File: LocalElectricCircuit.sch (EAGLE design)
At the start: 43 parts, among them IC1 PIC32MX360F512L, J1 Prog. Port, J3 Prog. Port, T1 PN100, U1 ADS1118, U2 ADS1118

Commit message: 🗡️🗡️🗡️
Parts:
- added PIC16_POWER_EN, PIC32_POWER_EN: (no value), pinhead:PINHD-1X2
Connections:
- removed net +3V3_PROG: J1.2, R3.1
- new net PIC32_3V3: C1.1, C12.1, C13.1, C14.1, C15.1, C16.1, C2.1, C4.1, C5.1, C6.1, IC1.VDD@1, IC1.VDD@2, IC1.VDD@3, IC1.VDD@4, IC1.VDD@5, J1.2, PIC32_POWER_EN.1, R2.1, R3.1
- net +3V3: now also PIC16_POWER_EN.2, PIC32_POWER_EN.2; no longer C1.1, C12.1, C13.1, C14.1, C15.1, C16.1, C2.1, C4.1, C5.1, C6.1, IC1.VDD@1, IC1.VDD@2, IC1.VDD@3, IC1.VDD@4, IC1.VDD@5, R2.1
- net PIC16_3V3: now also PIC16_POWER_EN.1

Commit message: GND planes and some layout bizz
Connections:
- removed net GND_I_1: J2.A5
- removed net GND_I_2: J2.A6
- removed net GND_I_3: J2.A7
- removed net GND_PROBE: J2.B11, J2.B12, J2.B13, U1.AIN3, U2.AIN3
- new net GND: J2.A5, J2.A6, J2.A7, J2.B11, J2.B12, J2.B13, U1.AIN3, U2.AIN3
- new net PIC_3V3: IC1.VREG
- net +3V3: no longer IC1.VREG
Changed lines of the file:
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@@
 <setting verticaltext="up"/>
 </settings>
-<grid distance="0.1" unitdist="inch" unit="inch" style="lines" multiple="1" display="no" altdistance="0.025" altunitdist="inch" altunit="inch"/>
+<grid distance="0.1" unitdist="inch" unit="inch" style="lines" multiple="1" display="no" altdistance="0.01" altunitdist="inch" altunit="inch"/>
 <layers>
 <layer number="1" name="Top" color="4" fill="1" visible="no" active="no"/>
@@
 </segment>
 <segment>
-<pinref part="IC1" gate="G$1" pin="VREG"/>
-<wire x1="76.2" y1="114.3" x2="76.2" y2="124.46" width="0.1524" layer="91"/>
-<label x="76.835" y="124.46" size="1.778" layer="95" rot="R90"/>
-</segment>
-<segment>
 <pinref part="J2" gate="G$1" pin="B1"/>
 <wire x1="-45.72" y1="172.72" x2="-55.88" y2="172.72" width="0.1524" layer="91"/>
@@
 </segment>
 </net>
-<net name="GND_I_1" class="0">
+<net name="I_1_L" class="0">
+<segment>
+<pinref part="J2" gate="G$1" pin="B5"/>
+<wire x1="-45.72" y1="142.24" x2="-76.2" y2="142.24" width="0.1524" layer="91"/>
+<label x="-76.2" y="142.875" size="1.778" layer="95" rot="R180"/>
+</segment>
+<segment>
+<pinref part="IC1" gate="G$1" pin="RB4"/>
+<wire x1="17.78" y1="40.64" x2="7.62" y2="40.64" width="0.1524" layer="91"/>
+<label x="0" y="40.64" size="1.778" layer="95"/>
+</segment>
+</net>
+<net name="I_1_H" class="0">
+<segment>
+<pinref part="J2" gate="G$1" pin="C5"/>
+<wire x1="-45.72" y1="139.7" x2="-76.2" y2="139.7" width="0.1524" layer="91"/>
+<label x="-76.2" y="140.335" size="1.778" layer="95" rot="R180"/>
+</segment>
+<segment>
+<pinref part="IC1" gate="G$1" pin="RB5"/>
+<wire x1="17.78" y1="43.18" x2="7.62" y2="43.18" width="0.1524" layer="91"/>
+<label x="0" y="43.18" size="1.778" layer="95"/>
+</segment>
+</net>
+<net name="I_2_L" class="0">
+<segment>
+<pinref part="J2" gate="G$1" pin="B6"/>
+<wire x1="-45.72" y1="134.62" x2="-76.2" y2="134.62" width="0.1524" layer="91"/>
+<label x="-76.2" y="135.255" size="1.778" layer="95" rot="R180"/>
+</segment>
+<segment>
+<pinref part="IC1" gate="G$1" pin="RB8"/>
+<wire x1="55.88" y1="7.62" x2="55.88" y2="-7.62" width="0.1524" layer="91"/>
+<label x="55.88" y="-15.24" size="1.778" layer="95" rot="R90"/>
+</segment>
+</net>
+<net name="I_2_H" class="0">
+<segment>
+<pinref part="J2" gate="G$1" pin="C6"/>
+<wire x1="-45.72" y1="132.08" x2="-76.2" y2="132.08" width="0.1524" layer="91"/>
+<label x="-76.2" y="132.715" size="1.778" layer="95" rot="R180"/>
+</segment>
+<segment>
+<pinref part="IC1" gate="G$1" pin="RB9"/>
+<wire x1="58.42" y1="7.62" x2="58.42" y2="-7.62" width="0.1524" layer="91"/>
+<label x="58.42" y="-15.24" size="1.778" layer="95" rot="R90"/>
+</segment>
+</net>
+<net name="I_3_L" class="0">
+<segment>
+<pinref part="J2" gate="G$1" pin="B7"/>
+<wire x1="-45.72" y1="127" x2="-76.2" y2="127" width="0.1524" layer="91"/>
+<label x="-76.2" y="127.635" size="1.778" layer="95" rot="R180"/>
+</segment>
+<segment>
+<pinref part="IC1" gate="G$1" pin="RB10"/>
+<wire x1="60.96" y1="7.62" x2="60.96" y2="-7.62" width="0.1524" layer="91"/>
+<label x="60.96" y="-15.24" size="1.778" layer="95" rot="R90"/>
+</segment>
+</net>
+<net name="I_3_H" class="0">
+<segment>
+<pinref part="J2" gate="G$1" pin="C7"/>
+<wire x1="-45.72" y1="124.46" x2="-76.2" y2="124.46" width="0.1524" layer="91"/>
+<label x="-76.2" y="125.095" size="1.778" layer="95" rot="R180"/>
+</segment>
+<segment>
+<pinref part="IC1" gate="G$1" pin="RB11"/>
+<wire x1="63.5" y1="7.62" x2="63.5" y2="-7.62" width="0.1524" layer="91"/>
+<label x="63.5" y="-15.24" size="1.778" layer="95" rot="R90"/>
+</segment>
+</net>
+<net name="GND" class="0">
+<segment>
+<pinref part="U1" gate="G$1" pin="AIN3"/>
+<wire x1="236.22" y1="104.14" x2="259.08" y2="104.14" width="0.1524" layer="91"/>
+<label x="259.08" y="103.505" size="1.778" layer="95"/>
+</segment>
+<segment>
+<pinref part="U2" gate="G$1" pin="AIN3"/>
+<wire x1="236.22" y1="66.04" x2="259.08" y2="66.04" width="0.1524" layer="91"/>
+<label x="259.08" y="65.405" size="1.778" layer="95"/>
+</segment>
+<segment>
+<pinref part="J2" gate="G$1" pin="B11"/>
+<wire x1="-45.72" y1="96.52" x2="-55.88" y2="96.52" width="0.1524" layer="91"/>
+<label x="-55.88" y="97.155" size="1.778" layer="95" rot="R180"/>
+</segment>
+<segment>
+<pinref part="J2" gate="G$1" pin="B12"/>
+<wire x1="-45.72" y1="88.9" x2="-55.88" y2="88.9" width="0.1524" layer="91"/>
+<label x="-55.88" y="89.535" size="1.778" layer="95" rot="R180"/>
+</segment>
+<segment>
+<pinref part="J2" gate="G$1" pin="B13"/>
+<wire x1="-45.72" y1="81.28" x2="-55.88" y2="81.28" width="0.1524" layer="91"/>
+<label x="-55.88" y="81.915" size="1.778" layer="95" rot="R180"/>
+</segment>
 <segment>
 <pinref part="J2" gate="G$1" pin="A5"/>
@@
 <label x="-76.2" y="145.415" size="1.778" layer="95" rot="R180"/>
 </segment>
-</net>
-<net name="I_1_L" class="0">
-<segment>
-<pinref part="J2" gate="G$1" pin="B5"/>
-<wire x1="-45.72" y1="142.24" x2="-76.2" y2="142.24" width="0.1524" layer="91"/>
-<label x="-76.2" y="142.875" size="1.778" layer="95" rot="R180"/>
-</segment>
-<segment>
-<pinref part="IC1" gate="G$1" pin="RB4"/>
-<wire x1="17.78" y1="40.64" x2="7.62" y2="40.64" width="0.1524" layer="91"/>
-<label x="0" y="40.64" size="1.778" layer="95"/>
-</segment>
-</net>
-<net name="I_1_H" class="0">
-<segment>
-<pinref part="J2" gate="G$1" pin="C5"/>
-<wire x1="-45.72" y1="139.7" x2="-76.2" y2="139.7" width="0.1524" layer="91"/>
-<label x="-76.2" y="140.335" size="1.778" layer="95" rot="R180"/>
-</segment>
-<segment>
-<pinref part="IC1" gate="G$1" pin="RB5"/>
-<wire x1="17.78" y1="43.18" x2="7.62" y2="43.18" width="0.1524" layer="91"/>
-<label x="0" y="43.18" size="1.778" layer="95"/>
-</segment>
-</net>
-<net name="GND_I_2" class="0">
 <segment>
 <pinref part="J2" gate="G$1" pin="A6"/>
@@
 <label x="-76.2" y="137.795" size="1.778" layer="95" rot="R180"/>
 </segment>
-</net>
-<net name="I_2_L" class="0">
-<segment>
-<pinref part="J2" gate="G$1" pin="B6"/>
-<wire x1="-45.72" y1="134.62" x2="-76.2" y2="134.62" width="0.1524" layer="91"/>
-<label x="-76.2" y="135.255" size="1.778" layer="95" rot="R180"/>
-</segment>
-<segment>
-<pinref part="IC1" gate="G$1" pin="RB8"/>
-<wire x1="55.88" y1="7.62" x2="55.88" y2="-7.62" width="0.1524" layer="91"/>
-<label x="55.88" y="-15.24" size="1.778" layer="95" rot="R90"/>
-</segment>
-</net>
-<net name="I_2_H" class="0">
-<segment>
-<pinref part="J2" gate="G$1" pin="C6"/>
-<wire x1="-45.72" y1="132.08" x2="-76.2" y2="132.08" width="0.1524" layer="91"/>
-<label x="-76.2" y="132.715" size="1.778" layer="95" rot="R180"/>
-</segment>
-<segment>
-<pinref part="IC1" gate="G$1" pin="RB9"/>
-<wire x1="58.42" y1="7.62" x2="58.42" y2="-7.62" width="0.1524" layer="91"/>
-<label x="58.42" y="-15.24" size="1.778" layer="95" rot="R90"/>
-</segment>
-</net>
-<net name="GND_I_3" class="0">
 <segment>
 <pinref part="J2" gate="G$1" pin="A7"/>
 <wire x1="-45.72" y1="129.54" x2="-76.2" y2="129.54" width="0.1524" layer="91"/>
 <label x="-76.2" y="130.175" size="1.778" layer="95" rot="R180"/>
-</segment>
-</net>
-<net name="I_3_L" class="0">
-<segment>
-<pinref part="J2" gate="G$1" pin="B7"/>
-<wire x1="-45.72" y1="127" x2="-76.2" y2="127" width="0.1524" layer="91"/>
-<label x="-76.2" y="127.635" size="1.778" layer="95" rot="R180"/>
-</segment>
-<segment>
-<pinref part="IC1" gate="G$1" pin="RB10"/>
-<wire x1="60.96" y1="7.62" x2="60.96" y2="-7.62" width="0.1524" layer="91"/>
-<label x="60.96" y="-15.24" size="1.778" layer="95" rot="R90"/>
-</segment>
-</net>
-<net name="I_3_H" class="0">
-<segment>
-<pinref part="J2" gate="G$1" pin="C7"/>
-<wire x1="-45.72" y1="124.46" x2="-76.2" y2="124.46" width="0.1524" layer="91"/>
-<label x="-76.2" y="125.095" size="1.778" layer="95" rot="R180"/>
-</segment>
-<segment>
-<pinref part="IC1" gate="G$1" pin="RB11"/>
-<wire x1="63.5" y1="7.62" x2="63.5" y2="-7.62" width="0.1524" layer="91"/>
-<label x="63.5" y="-15.24" size="1.778" layer="95" rot="R90"/>
-</segment>
-</net>
-<net name="GND_PROBE" class="0">
-<segment>
-<pinref part="U1" gate="G$1" pin="AIN3"/>
-<wire x1="236.22" y1="104.14" x2="259.08" y2="104.14" width="0.1524" layer="91"/>
-<label x="259.08" y="103.505" size="1.778" layer="95"/>
-</segment>
-<segment>
-<pinref part="U2" gate="G$1" pin="AIN3"/>
-<wire x1="236.22" y1="66.04" x2="259.08" y2="66.04" width="0.1524" layer="91"/>
-<label x="259.08" y="65.405" size="1.778" layer="95"/>
-</segment>
-<segment>
-<pinref part="J2" gate="G$1" pin="B11"/>
-<wire x1="-45.72" y1="96.52" x2="-55.88" y2="96.52" width="0.1524" layer="91"/>
-<label x="-55.88" y="97.155" size="1.778" layer="95" rot="R180"/>
-</segment>
-<segment>
-<pinref part="J2" gate="G$1" pin="B12"/>
-<wire x1="-45.72" y1="88.9" x2="-55.88" y2="88.9" width="0.1524" layer="91"/>
-<label x="-55.88" y="89.535" size="1.778" layer="95" rot="R180"/>
-</segment>
-<segment>
-<pinref part="J2" gate="G$1" pin="B13"/>
-<wire x1="-45.72" y1="81.28" x2="-55.88" y2="81.28" width="0.1524" layer="91"/>
-<label x="-55.88" y="81.915" size="1.778" layer="95" rot="R180"/>
 </segment>
 </net>
@@
 </segment>
 </net>
+<net name="PIC_3V3" class="0">
+<segment>
+<pinref part="IC1" gate="G$1" pin="VREG"/>
+<wire x1="76.2" y1="114.3" x2="76.2" y2="116.84" width="0.1524" layer="91"/>
+<label x="76.835" y="116.84" size="1.778" layer="95" rot="R90"/>
+</segment>
+</net>

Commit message: It's a healthy baby board!
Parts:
- added R15: 1k, rcl:R-US_0309/12
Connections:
- removed net PIC32_3V3: C1.1, C12.1, C13.1, C14.1, C15.1, C16.1, C2.1, C4.1, C5.1, C6.1, IC1.VDD@1, IC1.VDD@2, IC1.VDD@3, IC1.VDD@4, IC1.VDD@5, J1.2, PIC32_POWER_EN.1, R2.1, R3.1
- new net N$10: R15.1, T1.B
- net +3V3: now also C1.1, C12.1, C13.1, C14.1, C15.1, C16.1, C2.1, C4.1, C5.1, C6.1, IC1.VDD@1, IC1.VDD@2, IC1.VDD@3, IC1.VDD@4, IC1.VDD@5, J1.2, PIC32_POWER_EN.1, R2.1, R3.1
- net CONDUCTIVITY_ENABLE_3V: now also R15.2; no longer T1.B

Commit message: ✋✋✋✋✋hol' up hol' up ✋✋ looks 👀 like we got a master 🎓 memer 🐸🐸🐸 over here 👈👈👈
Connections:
- removed net PIC_3V3: IC1.VREG
- net +3V3: now also IC1.VREG
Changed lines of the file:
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@@
 </variantdefs>
 <classes>
-<class number="0" name="default" width="0" drill="0">
+<class number="0" name="default" width="0.2032" drill="0.3302">
+<clearance class="0" value="0.1524"/>
+</class>
+<class number="1" name="power" width="0.4064" drill="0.6096">
+<clearance class="1" value="0.3048"/>
 </class>
 </classes>
@@
 </segment>
 </net>
-<net name="+3V3" class="0">
+<net name="+3V3" class="1">
 <segment>
 <pinref part="U$1" gate="G$1" pin="3.3V"/>
@@
 <label x="93.98" y="170.18" size="1.778" layer="95" rot="R180"/>
 </segment>
-</net>
-<net name="GND_3V3" class="0">
+<segment>
+<pinref part="IC1" gate="G$1" pin="VREG"/>
+<wire x1="76.2" y1="114.3" x2="76.2" y2="116.84" width="0.1524" layer="91"/>
+<label x="76.835" y="116.84" size="1.778" layer="95" rot="R90"/>
+</segment>
+</net>
+<net name="GND_3V3" class="1">
 <segment>
 <pinref part="IC1" gate="G$1" pin="VSS@1"/>
@@
 </segment>
 </net>
-<net name="GND_5V" class="0">
+<net name="GND_5V" class="1">
 <segment>
 <pinref part="U1" gate="G$1" pin="GND"/>
@@
 </segment>
 </net>
-<net name="+5V" class="0">
+<net name="+5V" class="1">
 <segment>
 <pinref part="U1" gate="G$1" pin="VDD"/>
@@
 </segment>
 </net>
-<net name="GND" class="0">
+<net name="GND" class="1">
 <segment>
 <pinref part="U1" gate="G$1" pin="AIN3"/>
@@
 </segment>
 </net>
-<net name="PIC16_3V3" class="0">
+<net name="PIC16_3V3" class="1">
 <segment>
 <pinref part="PIC16" gate="G$1" pin="1"/>
@@
 </segment>
 </net>
-<net name="PIC_3V3" class="0">
-<segment>
-<pinref part="IC1" gate="G$1" pin="VREG"/>
-<wire x1="76.2" y1="114.3" x2="76.2" y2="116.84" width="0.1524" layer="91"/>
-<label x="76.835" y="116.84" size="1.778" layer="95" rot="R90"/>
-</segment>
-</net>

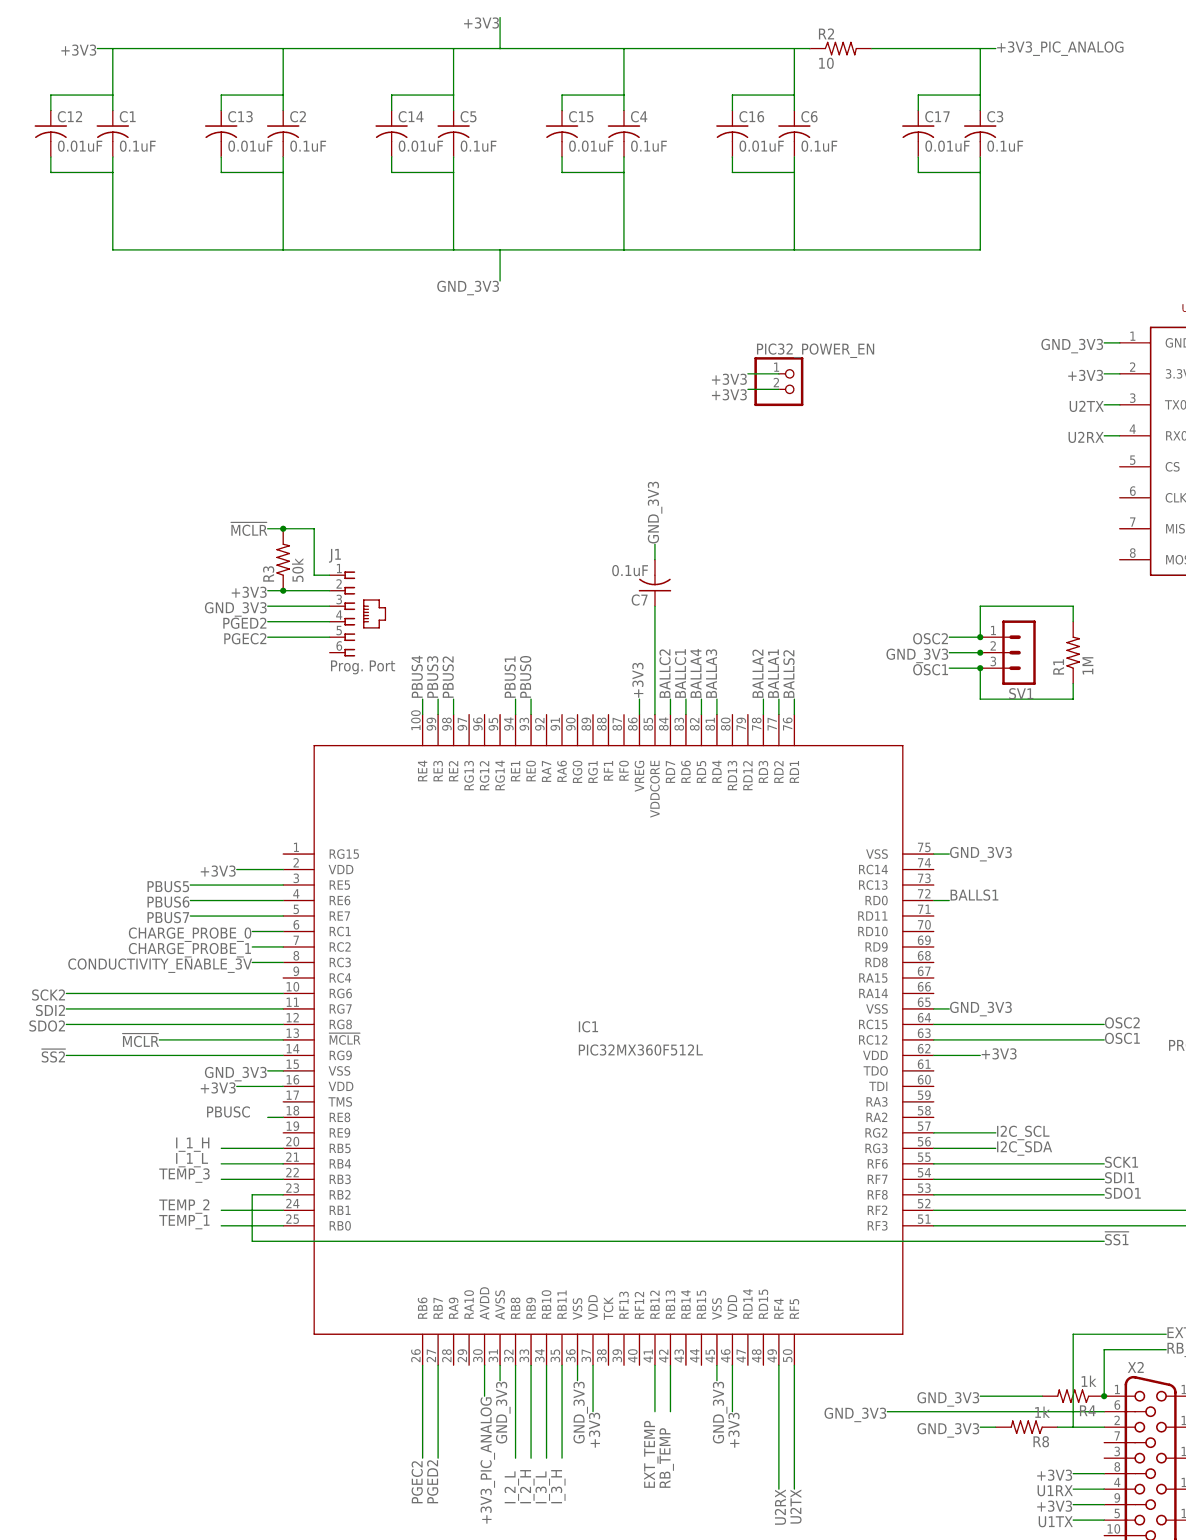
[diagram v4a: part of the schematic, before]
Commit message: Fixed a whole ton of issues from DRC Figured out there were vias stacked on eachother which caused 'Drill Distance' error Figured out that the radius around vias was set smaller than the general gap we were allowing, so it looked like the via would fit with its tStop/bStop, but it didn't leave 6mil between it and traces
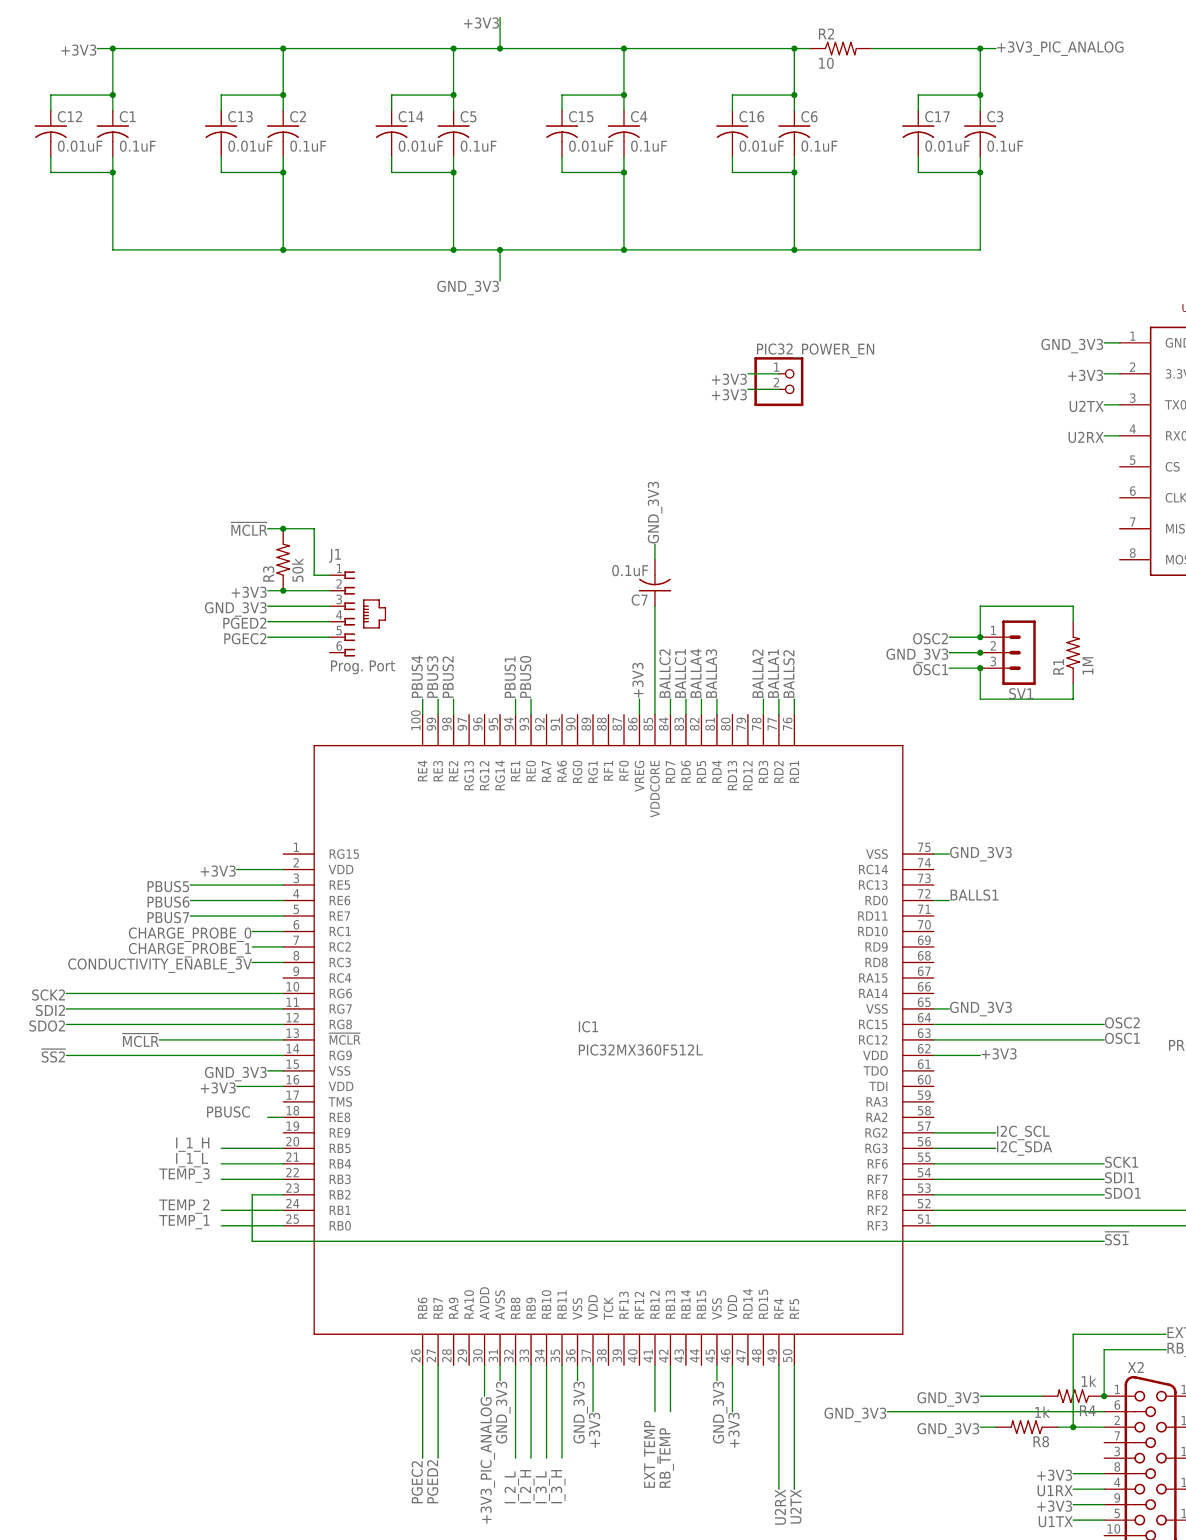
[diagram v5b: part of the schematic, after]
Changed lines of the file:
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@@
 <clearance class="0" value="0.1524"/>
 </class>
-<class number="1" name="power" width="0.4064" drill="0.6096">
-<clearance class="1" value="0.3048"/>
+<class number="1" name="power" width="0.4064" drill="0.3302">
+<clearance class="1" value="0.1524"/>
 </class>
 </classes>
@@
 <wire x1="91.44" y1="213.36" x2="91.44" y2="215.9" width="0.1524" layer="91"/>
 <wire x1="91.44" y1="215.9" x2="101.6" y2="215.9" width="0.1524" layer="91"/>
+<junction x="45.72" y="223.52"/>
+<junction x="101.6" y="223.52"/>
+<junction x="101.6" y="215.9"/>
+<junction x="73.66" y="215.9"/>
+<junction x="73.66" y="223.52"/>
+<junction x="-10.16" y="215.9"/>
+<junction x="17.78" y="215.9"/>
+<junction x="-10.16" y="223.52"/>
+<junction x="45.72" y="215.9"/>
+<junction x="53.34" y="223.52"/>
+<junction x="17.78" y="223.52"/>
 </segment>
 <segment>
@@
 <wire x1="121.92" y1="205.74" x2="121.92" y2="203.2" width="0.1524" layer="91"/>
 <wire x1="121.92" y1="203.2" x2="132.08" y2="203.2" width="0.1524" layer="91"/>
+<junction x="101.6" y="203.2"/>
+<junction x="73.66" y="203.2"/>
+<junction x="73.66" y="190.5"/>
+<junction x="45.72" y="190.5"/>
+<junction x="17.78" y="190.5"/>
+<junction x="-10.16" y="203.2"/>
+<junction x="17.78" y="203.2"/>
+<junction x="45.72" y="203.2"/>
+<junction x="132.08" y="203.2"/>
+<junction x="101.6" y="190.5"/>
+<junction x="53.34" y="190.5"/>
 </segment>
 <segment>
@@
 <wire x1="121.92" y1="213.36" x2="121.92" y2="215.9" width="0.1524" layer="91"/>
 <wire x1="121.92" y1="215.9" x2="132.08" y2="215.9" width="0.1524" layer="91"/>
+<junction x="132.08" y="223.52"/>
+<junction x="132.08" y="215.9"/>
 </segment>
 <segment>
@@
 <pinref part="X2" gate="G$1" pin="2"/>
 <wire x1="152.4" y1="-2.54" x2="147.32" y2="-2.54" width="0.1524" layer="91"/>
+<junction x="147.32" y="-2.54"/>
 </segment>
 </net>
@@
 </sheet>
 </sheets>
+<errors>
+</errors>
 </schematic>
 </drawing>
